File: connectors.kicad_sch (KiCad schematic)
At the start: 42 parts

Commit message: refactor labels U and assigned resistance footprint
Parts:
- R42, R43, R44, R45, R46, R47, R48, R49, R50, R51, R52: footprint (none) -> Resistor_SMD:R_0603_1608Metric
- U13: renamed from U14; value ~ -> HDGC1002WR-S-4P
- U14: renamed from U15; value ~ -> HDGC1002WR-S-4P
- U15: renamed from U16; value ~ -> HDGC1002WR-S-4P
- U16: renamed from U17; value ~ -> HDGC1002WR-S-4P
- U17: renamed from U29; value ~ -> HDGC1002WR-S-4P
- U18: renamed from U30; value ~ -> HDGC1002WR-S-4P
- U19: renamed from U31; value ~ -> HDGC1002WR-S-4P
- U20: renamed from U35; value ~ -> HDGC1002WR-S-8P
- U21: renamed from U34; value ~ -> HDGC1002WR-S-8P
- U22: renamed from U33; value ~ -> HDGC1002WR-S-6P
- U23: renamed from U32; value ~ -> HDGC1002WR-S-6P
- renumbered U18 to H1, U27 to H10, U28 to H11, U19 to H2, U20 to H3, U21 to H4, U22 to H5, U23 to H6, U24 to H7, U25 to H8, U26 to H9
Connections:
- net PWM_9: no longer R44.2
- new net PWM_10: R44.2
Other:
- note removed: "HDGC1002WR-S-4P"

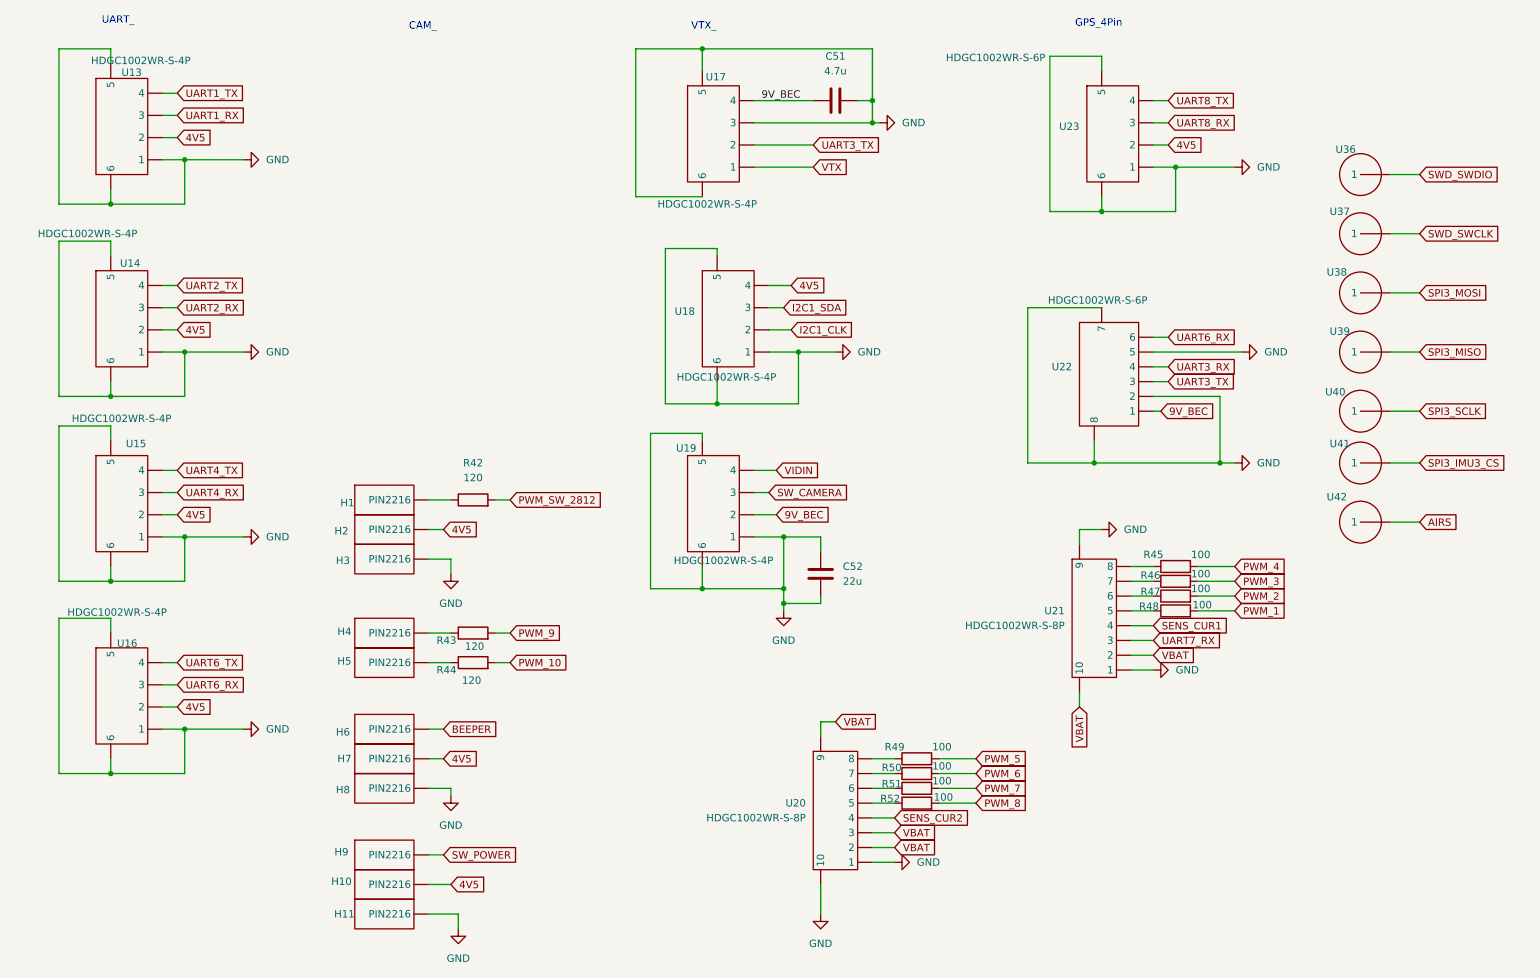
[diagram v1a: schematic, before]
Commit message: refactor and update references, added some footprints
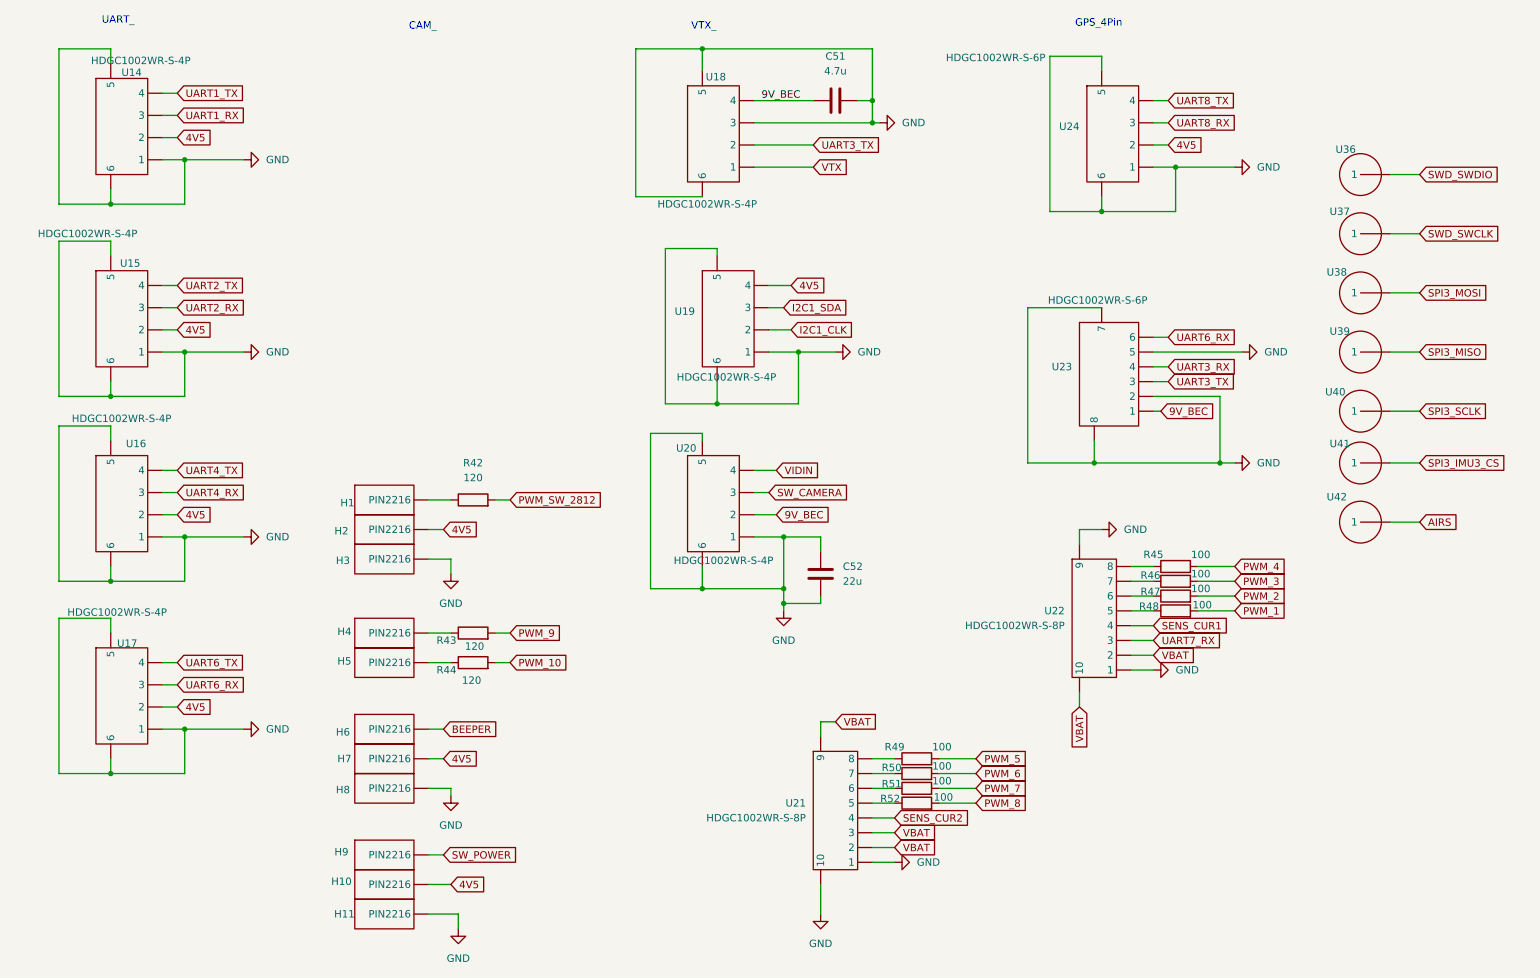
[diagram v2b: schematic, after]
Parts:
- C51: footprint (none) -> Capacitor_SMD:C_0805_2012Metric
- C52: footprint (none) -> Capacitor_SMD:C_1210_3225Metric
- renumbered U13 to U14, U14 to U15, U15 to U16, U16 to U17, U17 to U18, U18 to U19, U19 to U20, U20 to U21, U21 to U22, U22 to U23, U23 to U24
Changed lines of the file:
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@@
 		(on_board yes)
 		(dnp no)
-		(property "Reference" "U18"
+		(property "Reference" "U19"
 			(at 132.08 73.0249 0)
 			(effects
@@
 			(project "fch7"
 				(path "/11716af6-0e6e-444b-b738-3f12da23c1a2/304e7e23-68f8-4a1f-930d-8ec3265ffbba"
-					(reference "U18")
+					(reference "U19")
 					(unit 1)
 				)
@@
 		(on_board yes)
 		(dnp no)
-		(property "Reference" "U13"
+		(property "Reference" "U14"
 			(at 37.084 32.004 0)
 			(effects
@@
 			(project ""
 				(path "/11716af6-0e6e-444b-b738-3f12da23c1a2/304e7e23-68f8-4a1f-930d-8ec3265ffbba"
-					(reference "U13")
+					(reference "U14")
 					(unit 1)
 				)
@@
 		(on_board yes)
 		(dnp no)
-		(property "Reference" "U17"
+		(property "Reference" "U18"
 			(at 137.414 32.766 0)
 			(effects
@@
 			(project "fch7"
 				(path "/11716af6-0e6e-444b-b738-3f12da23c1a2/304e7e23-68f8-4a1f-930d-8ec3265ffbba"
-					(reference "U17")
+					(reference "U18")
 					(unit 1)
 				)
@@
 		(dnp no)
 		(fields_autoplaced yes)
-		(property "Reference" "U21"
+		(property "Reference" "U22"
 			(at 195.58 124.4599 0)
 			(effects
@@
 			(project ""
 				(path "/11716af6-0e6e-444b-b738-3f12da23c1a2/304e7e23-68f8-4a1f-930d-8ec3265ffbba"
-					(reference "U21")
+					(reference "U22")
 					(unit 1)
 				)
@@
 		(on_board yes)
 		(dnp no)
-		(property "Reference" "U15"
+		(property "Reference" "U16"
 			(at 37.846 95.758 0)
 			(effects
@@
 			(project "fch7"
 				(path "/11716af6-0e6e-444b-b738-3f12da23c1a2/304e7e23-68f8-4a1f-930d-8ec3265ffbba"
-					(reference "U15")
+					(reference "U16")
 					(unit 1)
 				)
@@
 			)
 		)
-		(property "Footprint" ""
+		(property "Footprint" "Capacitor_SMD:C_0805_2012Metric"
 			(at 160.02 35.8648 0)
 			(effects
@@
 		(on_board yes)
 		(dnp no)
-		(property "Reference" "U16"
+		(property "Reference" "U17"
 			(at 36.322 130.048 0)
 			(effects
@@
 			(project "fch7"
 				(path "/11716af6-0e6e-444b-b738-3f12da23c1a2/304e7e23-68f8-4a1f-930d-8ec3265ffbba"
-					(reference "U16")
+					(reference "U17")
 					(unit 1)
 				)
@@
 			)
 		)
-		(property "Footprint" ""
+		(property "Footprint" "Capacitor_SMD:C_1210_3225Metric"
 			(at 152.7048 114.3 0)
 			(effects
@@
 		(on_board yes)
 		(dnp no)
-		(property "Reference" "U19"
+		(property "Reference" "U20"
 			(at 132.334 96.52 0)
 			(effects
@@
 			(project "fch7"
 				(path "/11716af6-0e6e-444b-b738-3f12da23c1a2/304e7e23-68f8-4a1f-930d-8ec3265ffbba"
-					(reference "U19")
+					(reference "U20")
 					(unit 1)
 				)
@@
 		(dnp no)
 		(fields_autoplaced yes)
-		(property "Reference" "U20"
+		(property "Reference" "U21"
 			(at 151.13 157.4799 0)
 			(effects
@@
 			(project "fch7"
 				(path "/11716af6-0e6e-444b-b738-3f12da23c1a2/304e7e23-68f8-4a1f-930d-8ec3265ffbba"
-					(reference "U20")
+					(reference "U21")
 					(unit 1)
 				)
@@
 		(on_board yes)
 		(dnp no)
-		(property "Reference" "U23"
+		(property "Reference" "U24"
 			(at 198.12 41.2749 0)
 			(effects
@@
 			(project "fch7"
 				(path "/11716af6-0e6e-444b-b738-3f12da23c1a2/304e7e23-68f8-4a1f-930d-8ec3265ffbba"
-					(reference "U23")
+					(reference "U24")
 					(unit 1)
 				)
@@
 		(on_board yes)
 		(dnp no)
-		(property "Reference" "U14"
+		(property "Reference" "U15"
 			(at 36.83 64.77 0)
 			(effects
@@
 			(project "fch7"
 				(path "/11716af6-0e6e-444b-b738-3f12da23c1a2/304e7e23-68f8-4a1f-930d-8ec3265ffbba"
-					(reference "U14")
+					(reference "U15")
 					(unit 1)
 				)
@@
 		(on_board yes)
 		(dnp no)
-		(property "Reference" "U22"
+		(property "Reference" "U23"
 			(at 196.85 82.5499 0)
 			(effects
@@
 			(project ""
 				(path "/11716af6-0e6e-444b-b738-3f12da23c1a2/304e7e23-68f8-4a1f-930d-8ec3265ffbba"
-					(reference "U22")
+					(reference "U23")
 					(unit 1)
 				)
